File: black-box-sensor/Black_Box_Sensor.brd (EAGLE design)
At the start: 53 x 44 mm, 54 parts, among them J1 104031-0811, J2 UX60-MB-5S8, J3 B4B-PH-SM4-TBT(LF)(SN), U1 ADXL375, U2 ADXL375, U3 ATMEGA32U4-AU, U4 FXAS21002CQR1, U5 MIC5504-3.3YM5-TR, U6 NL27WZ32USG, U7 LT1129CST-5#PBF, U8 AD8426ACPZ-WP

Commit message: move things
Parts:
- removed U$1: TXU0304, BBS_Library:TSSOP14
- added U9: TXU0304, BBS_Library:TSSOP14
- moved U7 127.2 mm to (49.1, 39.9), turned to 270 degrees
- moved JP1 103.5 mm to (47.9, 14.5)
- moved R13 97.8 mm to (39.9, 31.8), flipped to the bottom
- moved R12 95.4 mm to (43.6, 31.8), flipped to the bottom
- moved R15 94.0 mm to (40.0, 17.7), flipped to the bottom
- moved R10 93.4 mm to (47.3, 31.9), flipped to the bottom
- moved R14 91.7 mm to (43.5, 17.7), flipped to the bottom
- moved C21 83.7 mm to (7.70, 1.00)
- moved R9 77.8 mm to (39.9, 22.9), flipped to the bottom
- moved R8 76.5 mm to (40.1, 26.1), flipped to the bottom
- moved R11 74.9 mm to (40.0, 29.0), flipped to the bottom
- moved R7 50.7 mm to (40.1, 14.9), flipped to the bottom
- moved R1 15.8 mm to (34.1, 34.4), flipped to the bottom, turned to 180 degrees
- moved R5 10.3 mm to (47.3, 26.1), flipped to the bottom
- moved C11 10.2 mm to (15.2, 35.4), flipped to the bottom, turned to 0 degrees
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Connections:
- net +5V: now also U9.14; no longer U$1.14
- net 3.3V: now also U9.1; no longer U$1.1
- net GND: now also U9.7; no longer U$1.7
- net MISO: now also U9.3; no longer U$1.3
- net MISO_5V: now also U9.12; no longer U$1.12
- net MOSI: now also U9.5; no longer U$1.5
- net MOSI_5V: now also U9.10; no longer U$1.10
- net OE: now also U9.8; no longer U$1.8
- net SCLK: now also U9.2; no longer U$1.2
- net SCLK_5V: now also U9.13; no longer U$1.13
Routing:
- net N$7: track 7.02 -> 9.90 mm
- net V-: track 4.89 -> 6.93 mm
- net V+: track 4.83 -> 6.82 mm
- net +5V: track 1.90 -> 1.35 mm
- net GND: track 1.03 -> 0.64 mm, vias 1 -> 2

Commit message: rout
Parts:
- moved C21 44.6 mm to (36.7, 34.9), flipped to the bottom
- moved U6 28.9 mm to (27.7, 17.1)
- moved LED2 26.3 mm to (19.4, 29.0), turned to 90 degrees
- moved R3 25.4 mm to (23.4, 32.7)
- moved U4 22.8 mm to (29.0, 23.8)
- moved J1 22.1 mm to (27.3, 6.68), turned to 180 degrees
- moved C6 21.4 mm to (30.5, 24.6)
- moved ISP1 19.2 mm to (46.4, 13.2), turned to 180 degrees
- moved U2 16.2 mm to (21.4, 15.8), turned to 90 degrees
- moved C3 15.6 mm to (19.1, 13.8), turned to 180 degrees
- moved U1 15.1 mm to (21.5, 23.8), turned to 90 degrees
- moved C11 14.5 mm to (18.9, 21.4), turned to 180 degrees
- moved C13 12.9 mm to (23.4, 27.8), turned to 0 degrees
- moved U7 12.7 mm to (36.4, 39.8)
- moved C5 12.5 mm to (27.8, 16.8), turned to 180 degrees
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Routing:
- net +5V: track 1.35 -> 63.4 mm, vias 0 -> 15
- net SCLK: track 0.00 -> 55.5 mm, vias 0 -> 5
- net CS2: track 0.00 -> 46.5 mm, vias 0 -> 3
- net MISO_5V: track 0.00 -> 42.7 mm, vias 0 -> 1
- net 3.3V: track 0.00 -> 41.5 mm, vias 0 -> 15
- net CS1: track 0.00 -> 40.6 mm, vias 0 -> 3
- net GND: track 0.64 -> 40.9 mm, vias 2 -> 18
- net MOSI_5V: track 0.00 -> 39.4 mm, vias 0 -> 4
- net MISO: track 0.00 -> 37.9 mm, vias 0 -> 2
- net MOSI: track 0.00 -> 37.8 mm, vias 0 -> 4
- net D-: track 0.00 -> 37.6 mm, vias 0 -> 1
- net LED: track 0.00 -> 37.0 mm, vias 0 -> 2
- net INT1: track 0.00 -> 26.9 mm, vias 0 -> 2
- net CS4: track 0.00 -> 24.8 mm, vias 0 -> 1
- net INT0: track 0.00 -> 24.5 mm, vias 0 -> 2
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- added copper zone on layer 1, net +5V

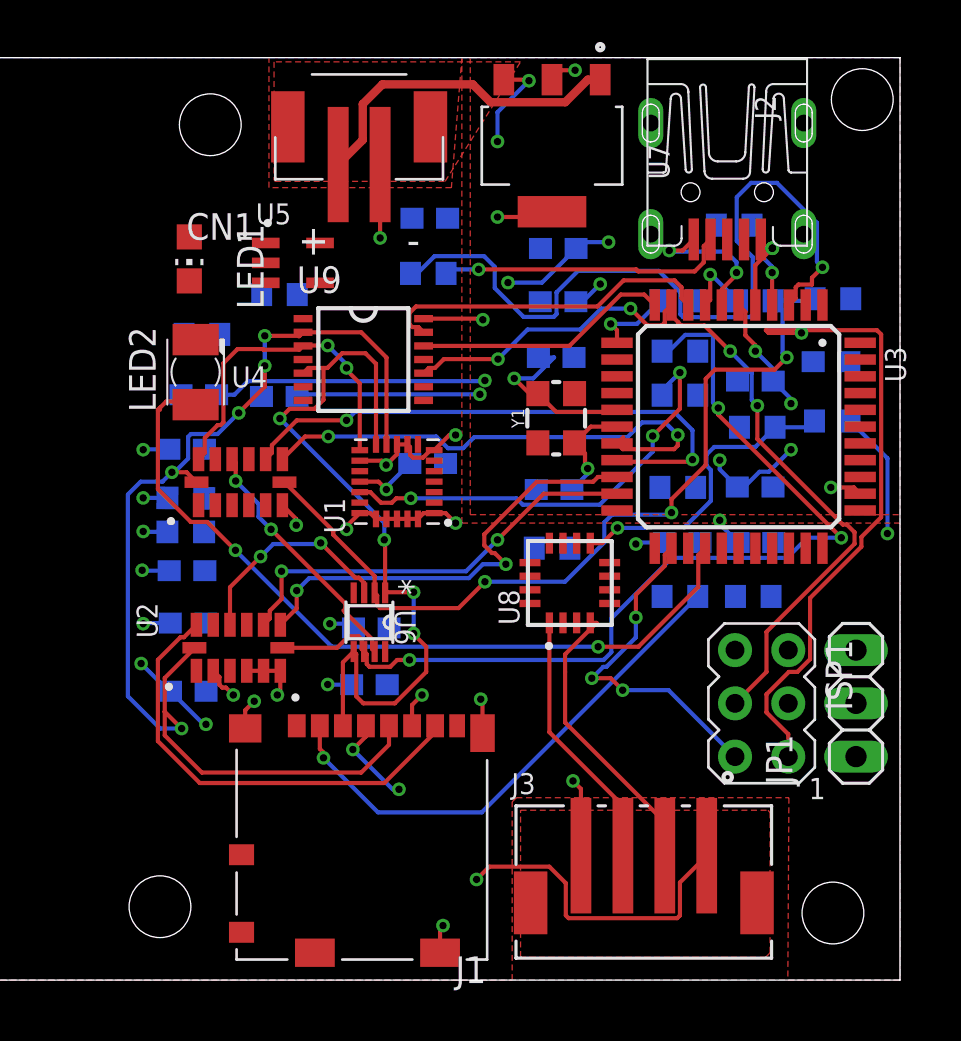
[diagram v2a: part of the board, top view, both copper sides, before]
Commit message: make it four layers and finish
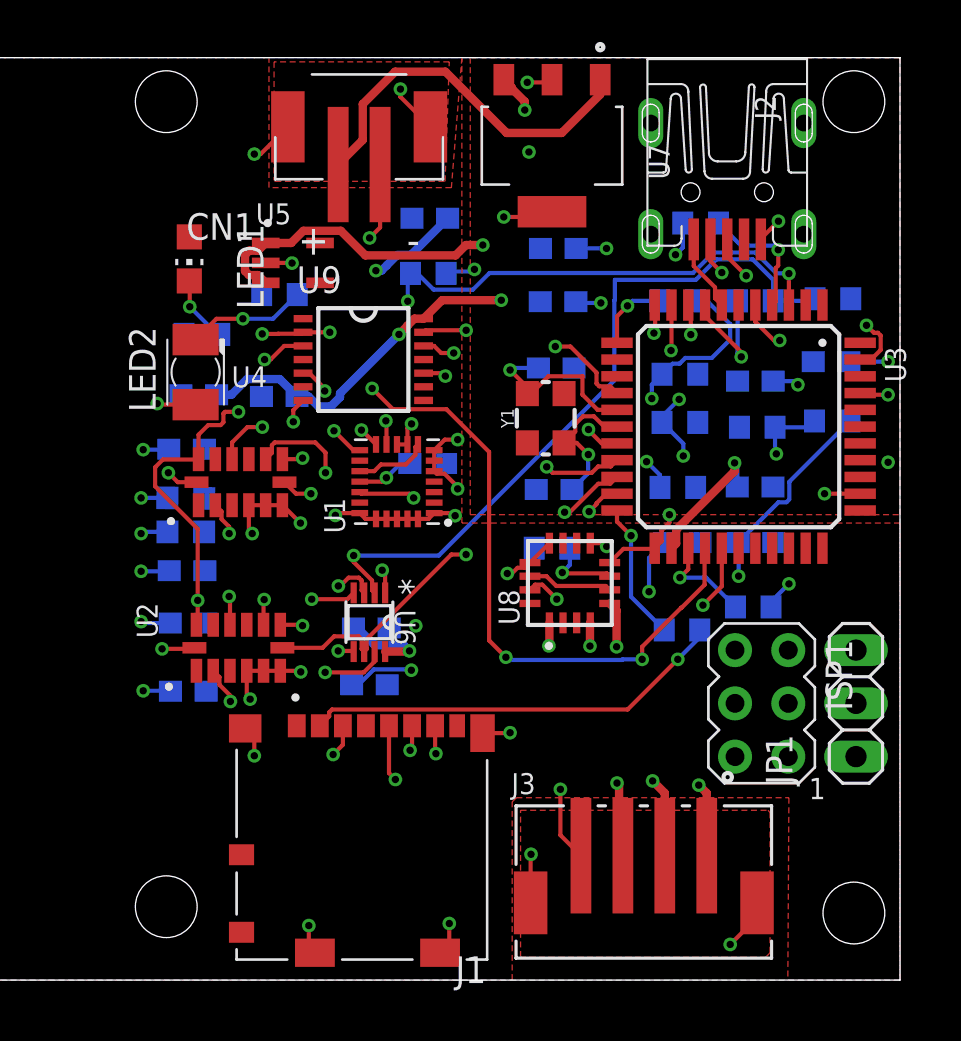
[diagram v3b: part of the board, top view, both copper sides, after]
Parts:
- moved R15 1.60 mm to (42.6, 16.7)
- moved R2 1.60 mm to (43.5, 36.1)
- moved R8 1.30 mm to (42.5, 26.6)
- moved R11 1.10 mm to (42.5, 28.9)
- moved C15 0.50 mm to (36.6, 29.2)
- moved R14 0.50 mm to (46.0, 17.8)
- moved Y1 0.50 mm to (36.1, 26.8)
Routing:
- net GND: track 40.9 -> 74.2 mm, vias 18 -> 34
- net SCLK_5V: track 16.1 -> 35.1 mm, vias 0 -> 2
- net RECEIVER: track 0.00 -> 17.5 mm, vias 0 -> 1
- net D-: track 37.6 -> 22.4 mm, vias 1 -> 2
- net CS2: track 46.5 -> 32.2 mm, vias 3 -> 2
- net CURRENT: track 0.00 -> 13.8 mm, vias 0 -> 2
- net MOSI: track 37.8 -> 25.3 mm, vias 4 -> 5
- net CS3: track 21.2 -> 32.2 mm, vias 3 -> 4
- net CS4: track 24.8 -> 34.1 mm, vias 1 -> 2
- net SCLK: track 55.5 -> 46.3 mm, vias 5 -> 6
- net 3.3V: track 41.5 -> 49.7 mm, vias 15 -> 13
- net N$2: track 0.00 -> 7.94 mm, vias 0 -> 2
- net INT1: track 26.9 -> 19.4 mm
- net INT0: track 24.5 -> 17.0 mm
- net CS4_5V: track 0.00 -> 6.63 mm, vias 0 -> 1
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
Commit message: finish
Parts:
- moved C21 19.1 mm to (18.6, 41.0), turned to 180 degrees
- moved C17 15.8 mm to (11.9, 14.3)
- moved C16 15.8 mm to (33.9, 29.5)
- moved C18 15.8 mm to (30.3, 20.9)
- moved C9 15.8 mm to (30.3, 23.5)
- moved R5 15.8 mm to (34.0, 26.7)
- moved C10 15.8 mm to (30.3, 28.6)
- moved C11 15.8 mm to (3.13, 21.4)
- moved C12 15.8 mm to (3.13, 23.0)
- moved C13 15.8 mm to (7.59, 27.8)
- moved C15 15.8 mm to (20.8, 29.2)
- moved C19 15.8 mm to (26.8, 20.9)
- moved C2 15.8 mm to (14.8, 36.3)
- moved C20 15.8 mm to (20.7, 23.4)
- moved C3 15.8 mm to (3.25, 13.8)
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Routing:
- net +5V: track 69.1 -> 51.7 mm, vias 11 -> 10
- net 3.3V: track 49.7 -> 46.6 mm
- net GND: track 74.2 -> 77.2 mm
- net MOSI: track 25.3 -> 23.5 mm
- net CS4: track 34.1 -> 35.7 mm, vias 2 -> 3
- net VBATT: track 18.0 -> 16.9 mm
- net CS1: track 39.6 -> 39.0 mm
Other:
- board size 53 x 44 mm -> 37.2 x 44 mm

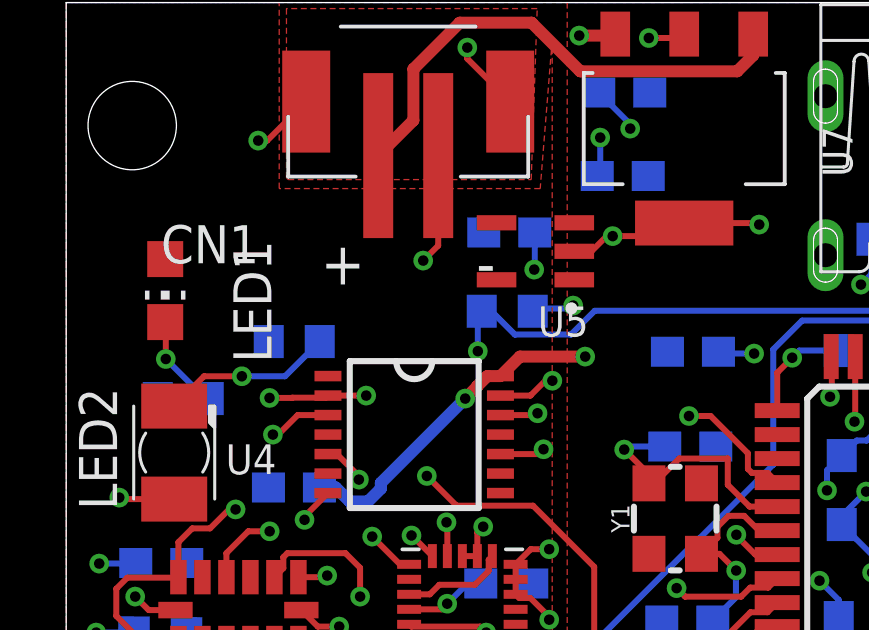
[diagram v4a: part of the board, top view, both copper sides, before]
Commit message: add capacitors to level shifter
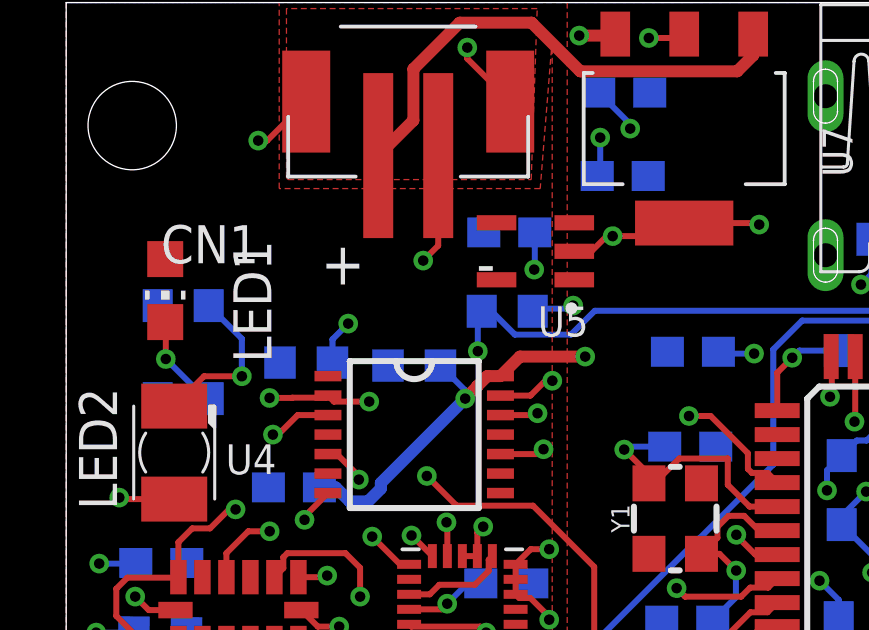
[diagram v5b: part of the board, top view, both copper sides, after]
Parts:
- added C22, C23: 0.1uF, rcl:C0603K
- moved R3 3.89 mm to (3.90, 33.9)
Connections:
- net +5V: now also C23.2
- net 3.3V: now also C22.2
- net GND: now also C22.1, C23.1
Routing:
- net 3.3V: track 46.6 -> 48.1 mm, vias 13 -> 14
- net +5V: track 51.7 -> 53.2 mm
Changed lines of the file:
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@@
 <drawing>
 <settings>
-<setting alwaysvectorfont="no"/>
+<setting alwaysvectorfont="yes"/>
 <setting verticaltext="up"/>
 </settings>
@@
 <hole x="35" y="4.1" drill="2.9464"/>
 <hole x="2.2" y="4.1" drill="2.9464"/>
+<dimension x1="0" y1="-0.2" x2="37.2" y2="-0.8" x3="18.6" y3="-0.8" textsize="1.778" layer="48" dtype="horizontal"/>
 </plain>
 <attributes>
@@
 <attribute name="VALUE" x="6.775" y="27.095" size="1.27" layer="27" rot="R90"/>
 </element>
-<element name="R3" library="rcl" library_urn="urn:adsk.eagle:library:334" package="R0603" package3d_urn="urn:adsk.eagle:package:23555/3" value="100" x="7.6" y="32.7" smashed="yes" rot="MR180">
-<attribute name="DJKPN" value="118-CR0603AFX-1000ELFCT-ND" x="7.6" y="32.7" size="1.778" layer="28" rot="MR180" display="off"/>
-<attribute name="NAME" x="6.965" y="32.065" size="1.27" layer="26" rot="MR180"/>
-<attribute name="POPULARITY" value="77" x="7.6" y="32.7" size="1.778" layer="28" rot="MR180" display="off"/>
-<attribute name="SPICEPREFIX" value="R" x="7.6" y="32.7" size="1.778" layer="28" rot="MR180" display="off"/>
-<attribute name="VALUE" x="6.965" y="34.605" size="1.27" layer="28" rot="MR180"/>
+<element name="R3" library="rcl" library_urn="urn:adsk.eagle:library:334" package="R0603" package3d_urn="urn:adsk.eagle:package:23555/3" value="100" x="3.9" y="33.9" smashed="yes" rot="MR180">
+<attribute name="DJKPN" value="118-CR0603AFX-1000ELFCT-ND" x="3.9" y="33.9" size="1.778" layer="28" rot="MR180" display="off"/>
+<attribute name="NAME" x="5.465" y="34.465" size="1.27" layer="26" rot="MR180"/>
+<attribute name="POPULARITY" value="77" x="3.9" y="33.9" size="1.778" layer="28" rot="MR180" display="off"/>
+<attribute name="SPICEPREFIX" value="R" x="3.9" y="33.9" size="1.778" layer="28" rot="MR180" display="off"/>
+<attribute name="VALUE" x="3.265" y="35.805" size="1.27" layer="28" rot="MR180"/>
 </element>
 <element name="R6" library="rcl" library_urn="urn:adsk.eagle:library:334" package="R0603" package3d_urn="urn:adsk.eagle:package:23555/3" value="100" x="3.9" y="30.8" smashed="yes" rot="MR0">
@@
 <attribute name="NAME" x="32.8" y="27.7" size="1.27" layer="25"/>
 <attribute name="VALUE" x="32.8" y="27.7" size="1.27" layer="27"/>
+</element>
+<element name="C22" library="rcl" library_urn="urn:adsk.eagle:library:334" package="C0603K" package3d_urn="urn:adsk.eagle:package:23680/2" value="0.1uF" x="8" y="32" smashed="yes" rot="MR180">
+<attribute name="NAME" x="7.2" y="31.35" size="1.016" layer="26" rot="MR180"/>
+<attribute name="POPULARITY" value="5" x="8" y="32" size="1.778" layer="28" rot="MR180" display="off"/>
+<attribute name="SPICEPREFIX" value="C" x="8" y="32" size="1.778" layer="28" rot="MR180" display="off"/>
+<attribute name="VALUE" x="7.2" y="33.65" size="1.016" layer="28" rot="MR180"/>
+</element>
+<element name="C23" library="rcl" library_urn="urn:adsk.eagle:library:334" package="C0603K" package3d_urn="urn:adsk.eagle:package:23680/2" value="0.1uF" x="11.6" y="31.9" smashed="yes" rot="MR180">
+<attribute name="NAME" x="10.8" y="31.25" size="1.016" layer="26" rot="MR180"/>
+<attribute name="POPULARITY" value="5" x="11.6" y="31.9" size="1.778" layer="28" rot="MR180" display="off"/>
+<attribute name="SPICEPREFIX" value="C" x="11.6" y="31.9" size="1.778" layer="28" rot="MR180" display="off"/>
+<attribute name="VALUE" x="10.8" y="33.55" size="1.016" layer="28" rot="MR180"/>
 </element>
 </elements>
@@
 <wire x1="10.375" y1="22.275" x2="10.2663875" y2="22.1663875" width="0.2" layer="1"/>
 <via x="10.2663875" y="22.1663875" extent="1-16" drill="0.35"/>
-<wire x1="20.6" y1="36.6504" x2="20.6496" y2="36.7" width="0.2" layer="1"/>
 <wire x1="20.6" y1="42.9496" x2="20.4704" y2="42.82" width="0.2" layer="1"/>
 <wire x1="20.4704" y1="42.82" x2="19.42" y2="42.82" width="0.2" layer="1"/>
@@
 <wire x1="23.0496" y1="36.6504" x2="23.1" y2="36.6" width="0.2" layer="1"/>
 <via x="23.1" y="36.6" extent="1-16" drill="0.35"/>
+<contactref element="C22" pad="1"/>
+<contactref element="C23" pad="1"/>
 </signal>
 <signal name="VBATT">
@@
 <wire x1="15.62" y1="35.12" x2="15.6" y2="35.1" width="0.2" layer="16"/>
 <via x="15.6" y="35.1" extent="1-16" drill="0.35"/>
+<contactref element="C22" pad="2"/>
+<wire x1="8.875" y1="32" x2="8.875" y2="32.775" width="0.2" layer="16"/>
+<wire x1="8.875" y1="32.775" x2="9.4" y2="33.3" width="0.2" layer="16"/>
+<via x="9.4" y="33.3" extent="1-16" drill="0.35"/>
 </signal>
 <signal name="N$1">
@@
 <wire x1="7.53041875" y1="30.822225" x2="7.53879375" y2="30.8306" width="0.2" layer="1"/>
 <wire x1="7.53879375" y1="30.8306" x2="8.6556" y2="30.8306" width="0.2" layer="1"/>
-<via x="10" y="30.9" extent="1-16" drill="0.35"/>
-<wire x1="10" y1="30.9" x2="10" y2="29.35085" width="0.2" layer="2"/>
-<wire x1="10" y1="29.35085" x2="12.675425" y2="26.675425" width="0.2" layer="2"/>
+<via x="10.1" y="30.7" extent="1-16" drill="0.35"/>
+<wire x1="10.1" y1="30.7" x2="10.1" y2="29.25085" width="0.2" layer="2"/>
+<wire x1="10.1" y1="29.25085" x2="12.675425" y2="26.675425" width="0.2" layer="2"/>
 <via x="12.675425" y="26.675425" extent="1-16" drill="0.35"/>
 <wire x1="12.675425" y1="26.675425" x2="12.705" y2="26.64585" width="0.2" layer="1"/>
@@
 <wire x1="2.3" y1="16.1" x2="2" y2="15.8" width="0.2" layer="2"/>
 <contactref element="U9" pad="2"/>
-<wire x1="10" y1="30.9" x2="8.725" y2="30.9" width="0.2" layer="1"/>
+<wire x1="10.1" y1="30.7" x2="8.925" y2="30.7" width="0.2" layer="1"/>
+<wire x1="8.925" y1="30.7" x2="8.725" y2="30.9" width="0.2" layer="1"/>
 <wire x1="8.725" y1="30.9" x2="8.6556" y2="30.8306" width="0.2" layer="1"/>
 </signal>
@@
 <wire x1="4.59445" y1="31.54445" x2="5.85555" y2="31.54445" width="0.2" layer="1"/>
 <via x="5.85555" y="31.54445" extent="1-16" drill="0.35"/>
-<wire x1="5.85555" y1="31.54445" x2="7.29445" y2="31.54445" width="0.2" layer="16"/>
-<wire x1="7.29445" y1="31.54445" x2="8.45" y2="32.7" width="0.2" layer="16"/>
+<wire x1="5.85555" y1="31.54445" x2="5.85555" y2="32.79445" width="0.2" layer="16"/>
+<wire x1="5.85555" y1="32.79445" x2="4.75" y2="33.9" width="0.2" layer="16"/>
 </signal>
 <signal name="N$6">
@@
 <wire x1="17.75" y1="41" x2="18.8" y2="39.95" width="0.2" layer="16"/>
 <wire x1="18.8" y1="39.95" x2="18.8" y2="39.8" width="0.2" layer="16"/>
+<contactref element="C23" pad="2"/>
+<wire x1="12.475" y1="31.9" x2="13.3" y2="31.075" width="0.2" layer="16"/>
+<wire x1="13.3" y1="31.075" x2="13.3" y2="30.8" width="0.2" layer="16"/>
 </signal>
 <signal name="MISO_5V">
